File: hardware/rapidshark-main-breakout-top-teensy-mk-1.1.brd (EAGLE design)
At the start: 35.6 x 17.8 mm, 17 parts, among them U1 TEENSY-3.1-OUTERPTH, U3 SN74LVC1T45SOT23-6

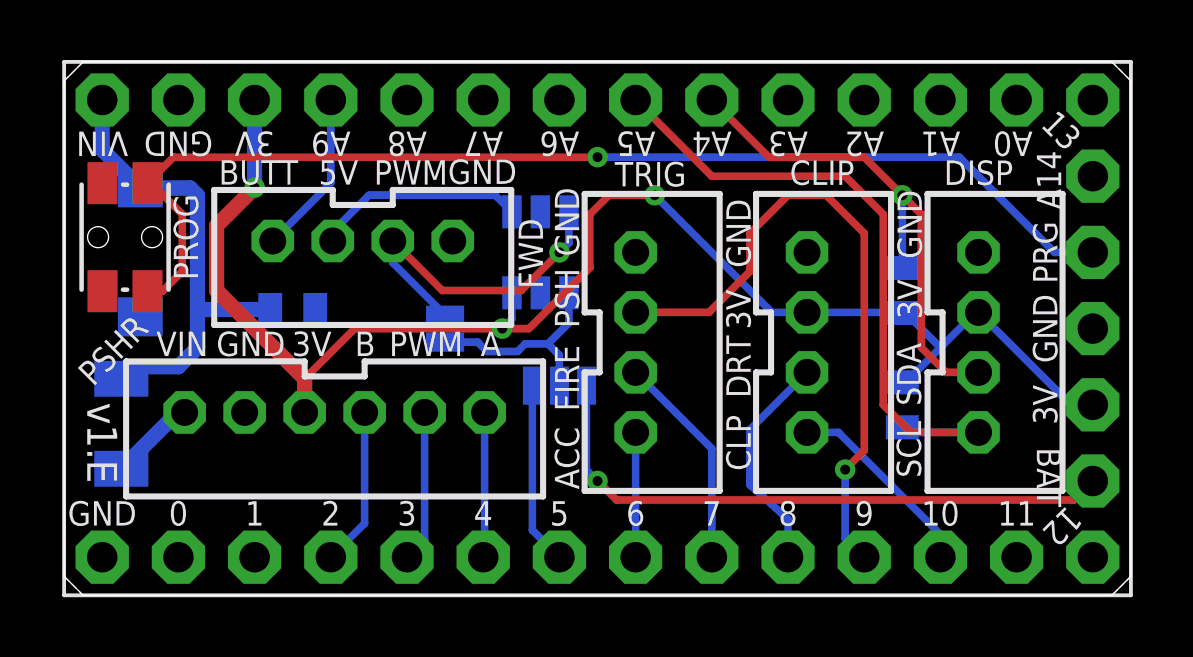
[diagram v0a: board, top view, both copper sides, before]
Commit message: new teensy lc mainboard with vreg
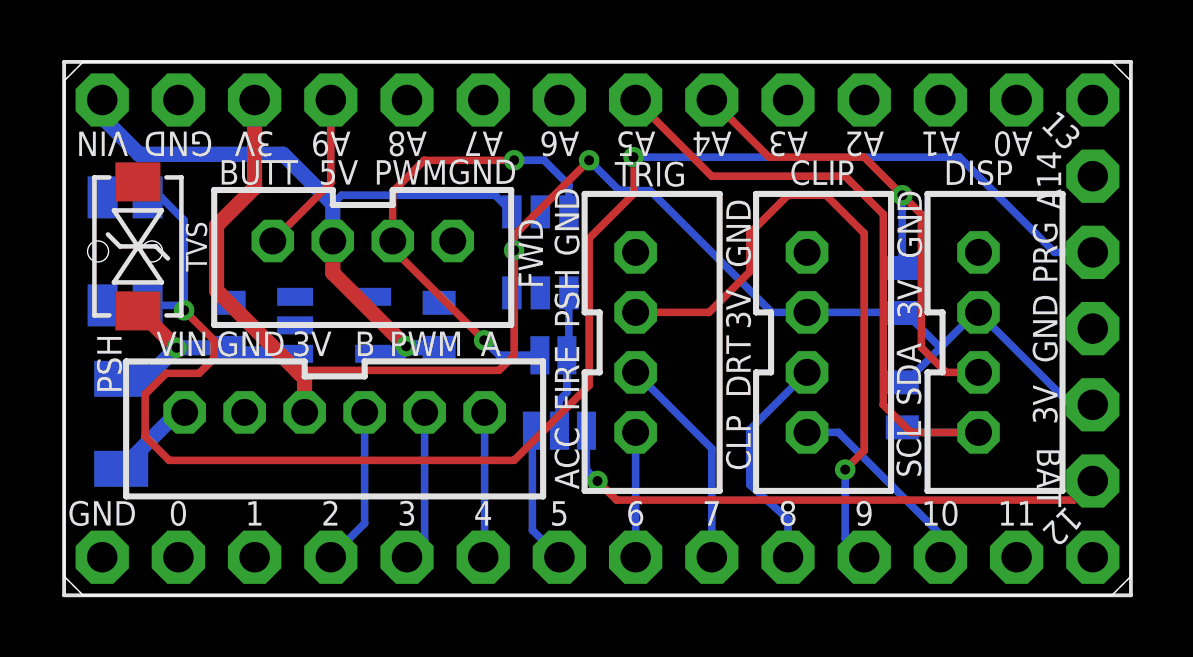
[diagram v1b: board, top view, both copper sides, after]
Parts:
- added C2: 2.2uF, a_parts:C0603-TIGHTER
- added U2: MIC5235, a_parts:SOT23-5
- moved BYPASS 3.72 mm to (16.3, 8.00), turned to 0 degrees
- moved C1 2.18 mm to (5.50, 9.00), turned to 90 degrees
- moved 3/17 1.50 mm to (16.5, 5.49)
- moved PROG 0.48 mm to (2.03, 11.5), flipped to the bottom, turned to 90 degrees
- moved TVS 0.22 mm to (2.46, 11.6), flipped to the top, turned to 270 degrees
- renumbered PSHR to PSH
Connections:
- net 5V: now also C2.1, U1.VIN, U2.5
- net GND: now also C2.2, U2.2
- net VIN: now also U2.1, U2.3; no longer U1.VIN
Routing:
- net 5V: track 7.02 -> 24.2 mm, vias 0 -> 1
- net PROG: track 38.1 -> 53.1 mm, vias 1 -> 2
- net VIN: track 15.9 -> 8.11 mm, vias 0 -> 1
- net ACCEL_PWM_5V: track 11.4 -> 15.8 mm, vias 1 -> 2
- net 3.3V: track 48.9 -> 51.4 mm, vias 3 -> 2
- net ACCEL_PWM: track 7.20 -> 4.73 mm
- net 5: track 6.09 -> 4.59 mm
- net 17: track 20.4 -> 18.9 mm
